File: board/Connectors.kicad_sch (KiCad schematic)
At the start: 17 parts, among them J12 SLOT 0, J13 SLOT 1, J14 SLOT 2, J15 SLOT 3, J16 SLOT 4, J17 SLOT 5, J18 SPI Device 0, J19 SPI Device 1, J20 SPI Device 2, J21 SPI Device 3, J22 SPI Device 4, J23 SPI Device 5, J24 SPI Device 6, J25 SPI Device 7, J26 Audio Jack, J27 VIA Port A, J28 SP720APP

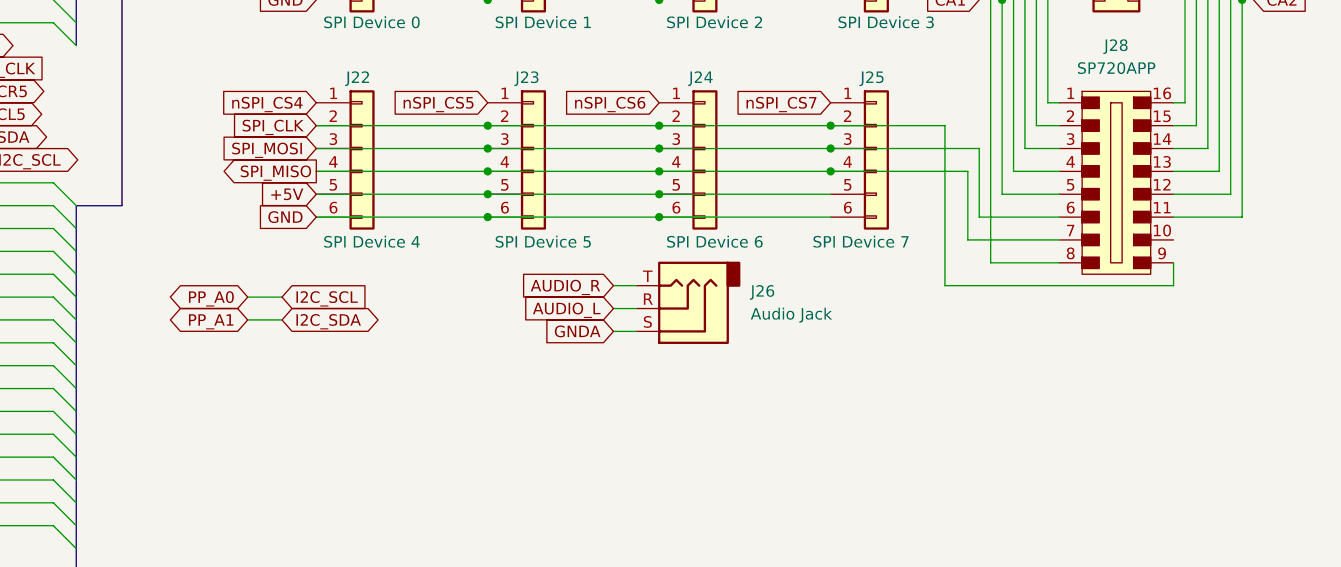
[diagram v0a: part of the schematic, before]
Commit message: V2.0 changes with new S register and simplified logic
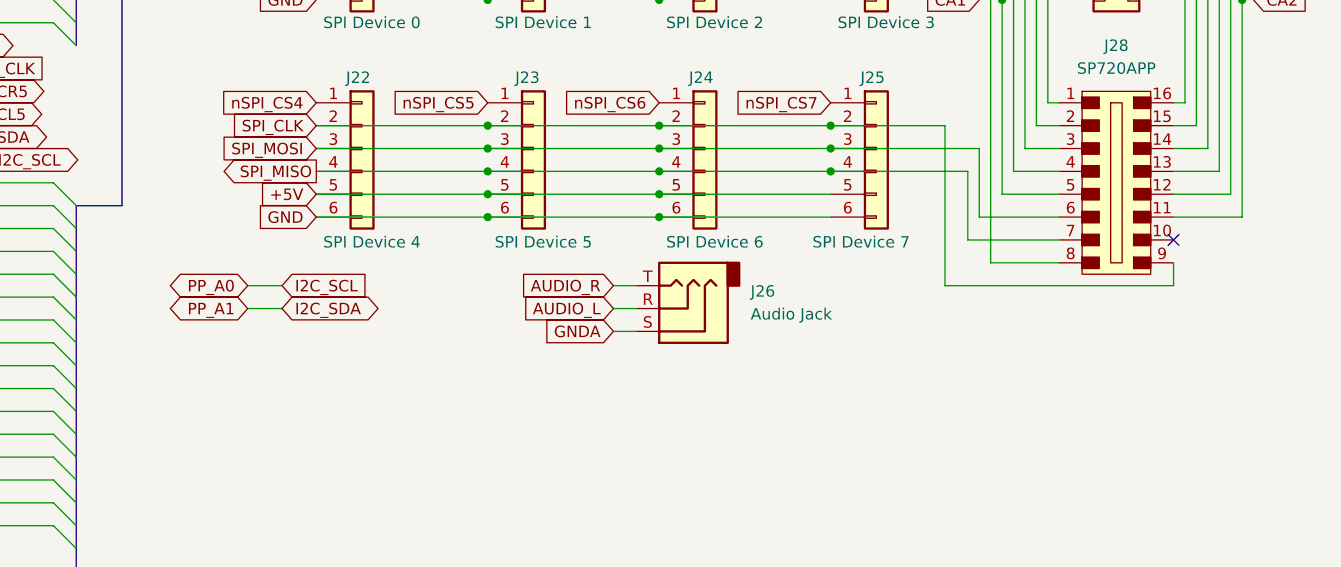
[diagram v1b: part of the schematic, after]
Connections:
- no-connect marks 0 -> 1
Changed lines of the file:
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@@
 		(title "Card-edge and SPI Device Connectors")
 		(date "2025-10-27")
-		(rev "1.8C")
+		(rev "2.0A")
 		(company "Data Tuning")
 		(comment 1 "Hydra 16")
@@
 		(color 0 0 0 0)
 	)
+	(no_connect
+		(at 247.65 157.48)
+	)
 	(bus_entry
 		(at 247.65 27.94)
@@
 	(wire
 		(pts
-			(xy 144.78 166.37) (xy 148.59 166.37)
+			(xy 144.78 165.1) (xy 148.59 165.1)
 		)
 		(stroke
@@
 	(wire
 		(pts
-			(xy 144.78 163.83) (xy 148.59 163.83)
+			(xy 144.78 162.56) (xy 148.59 162.56)
 		)
 		(stroke
@@
 	(global_label "PP_A1"
 		(shape bidirectional)
-		(at 144.78 166.37 180)
+		(at 144.78 165.1 180)
 		(fields_autoplaced yes)
 		(effects
@@
 		)
 		(property "Intersheetrefs" "${INTERSHEET_REFS}"
-			(at 134.8778 166.37 0)
+			(at 134.8778 165.1 0)
 			(effects
 				(font
@@
 	(global_label "PP_A0"
 		(shape bidirectional)
-		(at 144.78 163.83 180)
+		(at 144.78 162.56 180)
 		(fields_autoplaced yes)
 		(effects
@@
 		)
 		(property "Intersheetrefs" "${INTERSHEET_REFS}"
-			(at 134.8778 163.83 0)
+			(at 134.8778 162.56 0)
 			(effects
 				(font
@@
 	(global_label "I2C_SDA"
 		(shape bidirectional)
-		(at 148.59 166.37 0)
+		(at 148.59 165.1 0)
 		(fields_autoplaced yes)
 		(effects
@@
 		)
 		(property "Intersheetrefs" "${INTERSHEET_REFS}"
-			(at 160.3065 166.37 0)
+			(at 160.3065 165.1 0)
 			(effects
 				(font
@@
 	(global_label "I2C_SCL"
 		(shape input)
-		(at 148.59 163.83 0)
+		(at 148.59 162.56 0)
 		(fields_autoplaced yes)
 		(effects
@@
 		)
 		(property "Intersheetrefs" "${INTERSHEET_REFS}"
-			(at 159.1347 163.83 0)
+			(at 159.1347 162.56 0)
 			(effects
 				(font

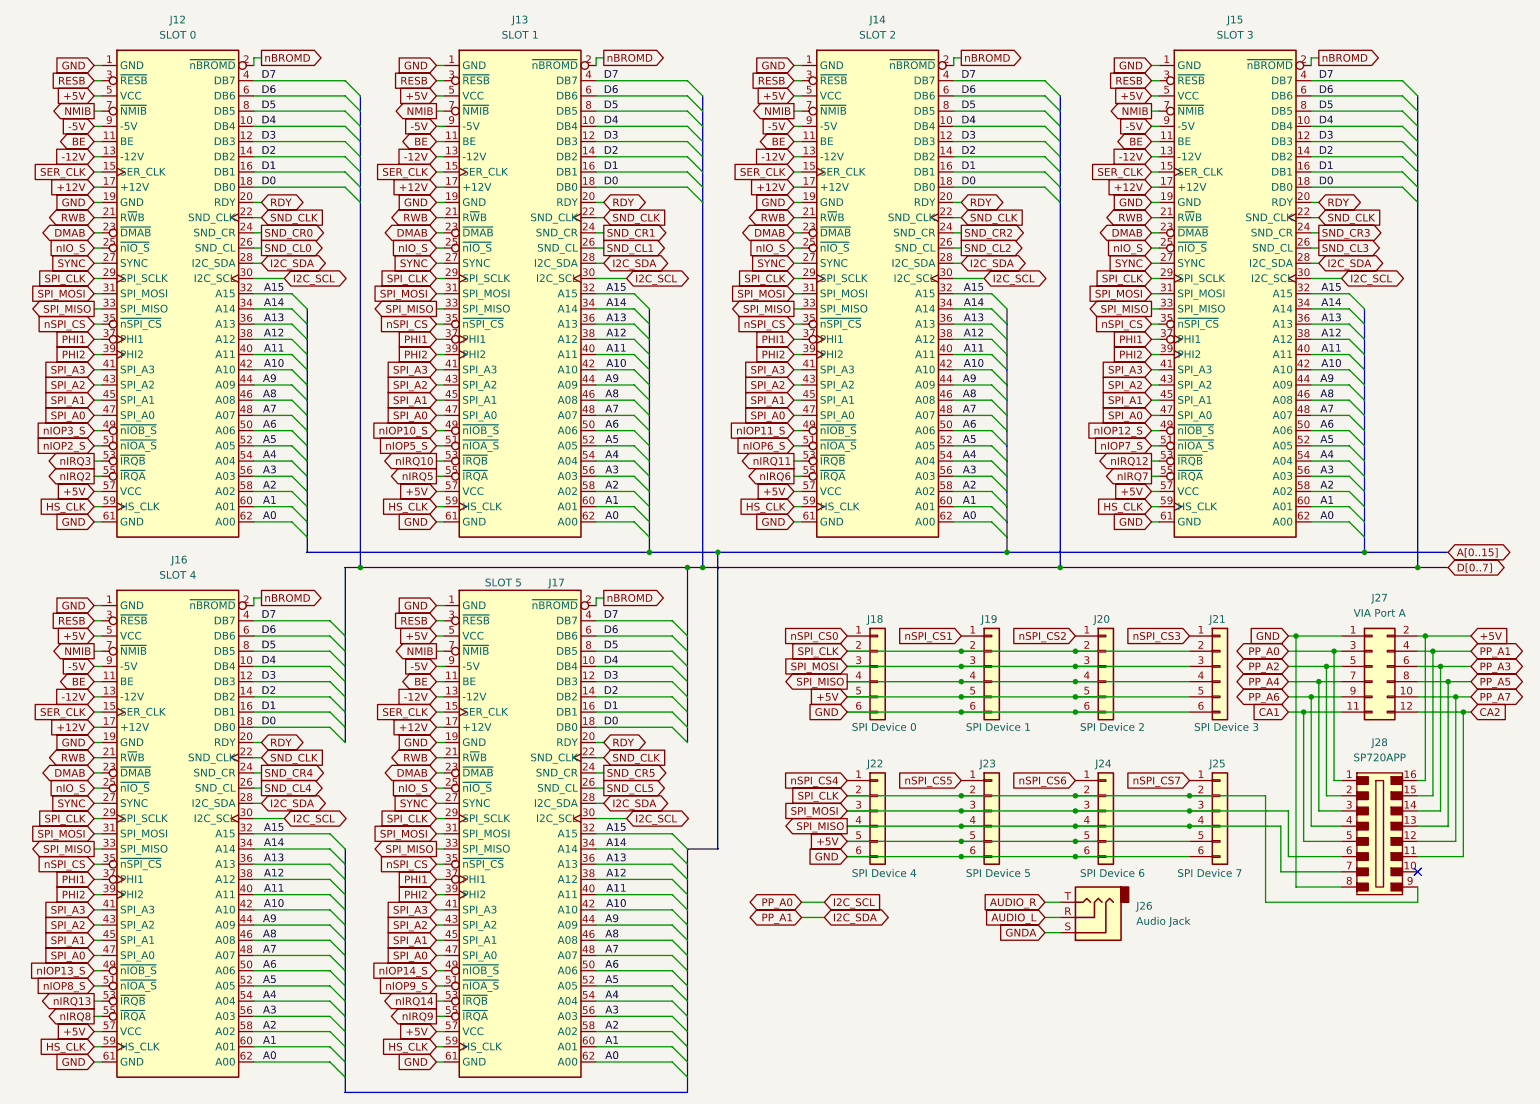
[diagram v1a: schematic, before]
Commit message: V2.0 updates and new hydra breakout and counter cards.
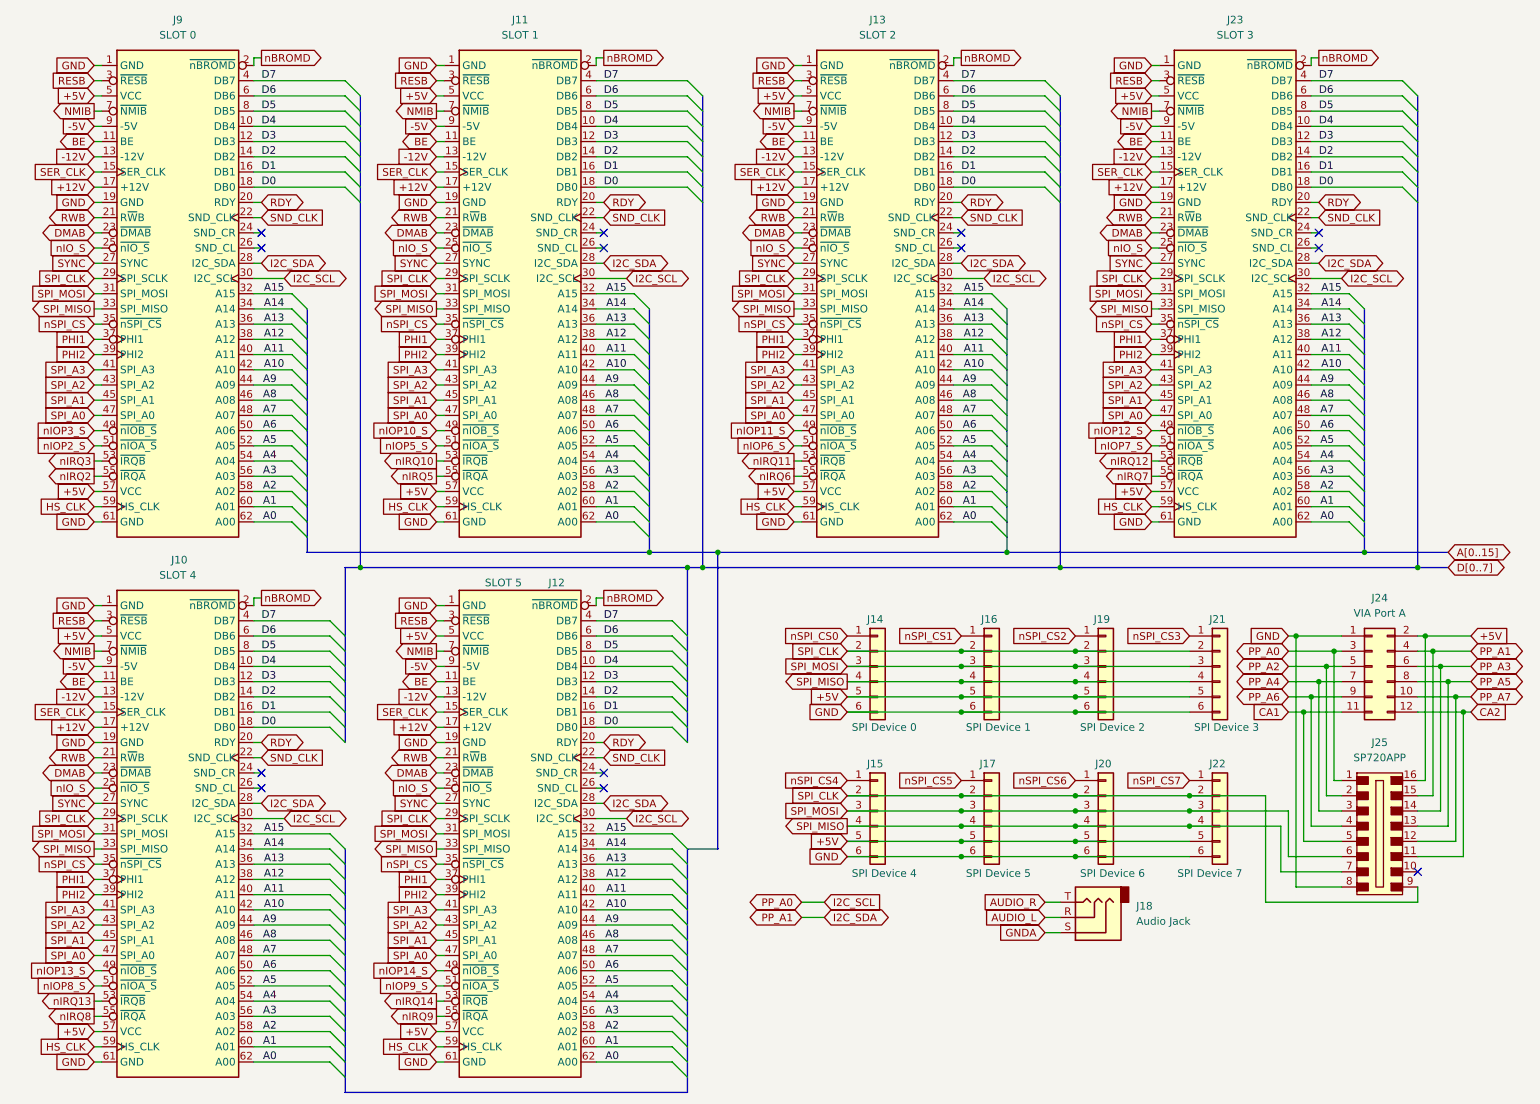
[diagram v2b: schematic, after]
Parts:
- renumbered J16 to J10, J13 to J11, J17 to J12, J14 to J13, J18 to J14, J22 to J15, J19 to J16, J23 to J17, J26 to J18, J20 to J19, J24 to J20, J25 to J22, J15 to J23, J27 to J24, J28 to J25, J12 to J9
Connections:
- net SND_CL0: no longer names the net of J9.26 (SND_CL)
- net SND_CL1: no longer names the net of J11.26 (SND_CL)
- net SND_CL2: no longer names the net of J13.26 (SND_CL)
- net SND_CL3: no longer names the net of J23.26 (SND_CL)
- net SND_CL4: no longer names the net of J10.26 (SND_CL)
- net SND_CL5: no longer names the net of J12.26 (SND_CL)
- net SND_CR0: no longer names the net of J9.24 (SND_CR)
- net SND_CR1: no longer names the net of J11.24 (SND_CR)
- net SND_CR2: no longer names the net of J13.24 (SND_CR)
- net SND_CR3: no longer names the net of J23.24 (SND_CR)
- net SND_CR4: no longer names the net of J10.24 (SND_CR)
- net SND_CR5: no longer names the net of J12.24 (SND_CR)
- no-connect marks 1 -> 13
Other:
- title: Card-edge and SPI Device Connectors -> ZeroPage $00/$01 Mirror Memory and RAM/ROM Bank Logic
